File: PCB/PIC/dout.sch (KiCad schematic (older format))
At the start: 63 parts, among them J10 TB_1X3, J11 TB_1X2, J12 TB_1X3, J13 TB_1X3, J14 TB_1X2, J15 TB_1X3, K1 RELAY_TE_1461353-2, K2 RELAY_TE_1461353-2, K3 RELAY_TE_1461353-2, K4 RELAY_TE_1461353-2, Q11 NDS7002A, Q12 NDS7002A, Q2 FQT13N06L, Q3 FQT13N06L, Q4 FQT13N06L, Q5 FQT13N06L, Q6 NDS7002A, Q7 NDS7002A, U23 MCP1416, U27 MCP1416, U28 MCP1416, U29 MCP1416

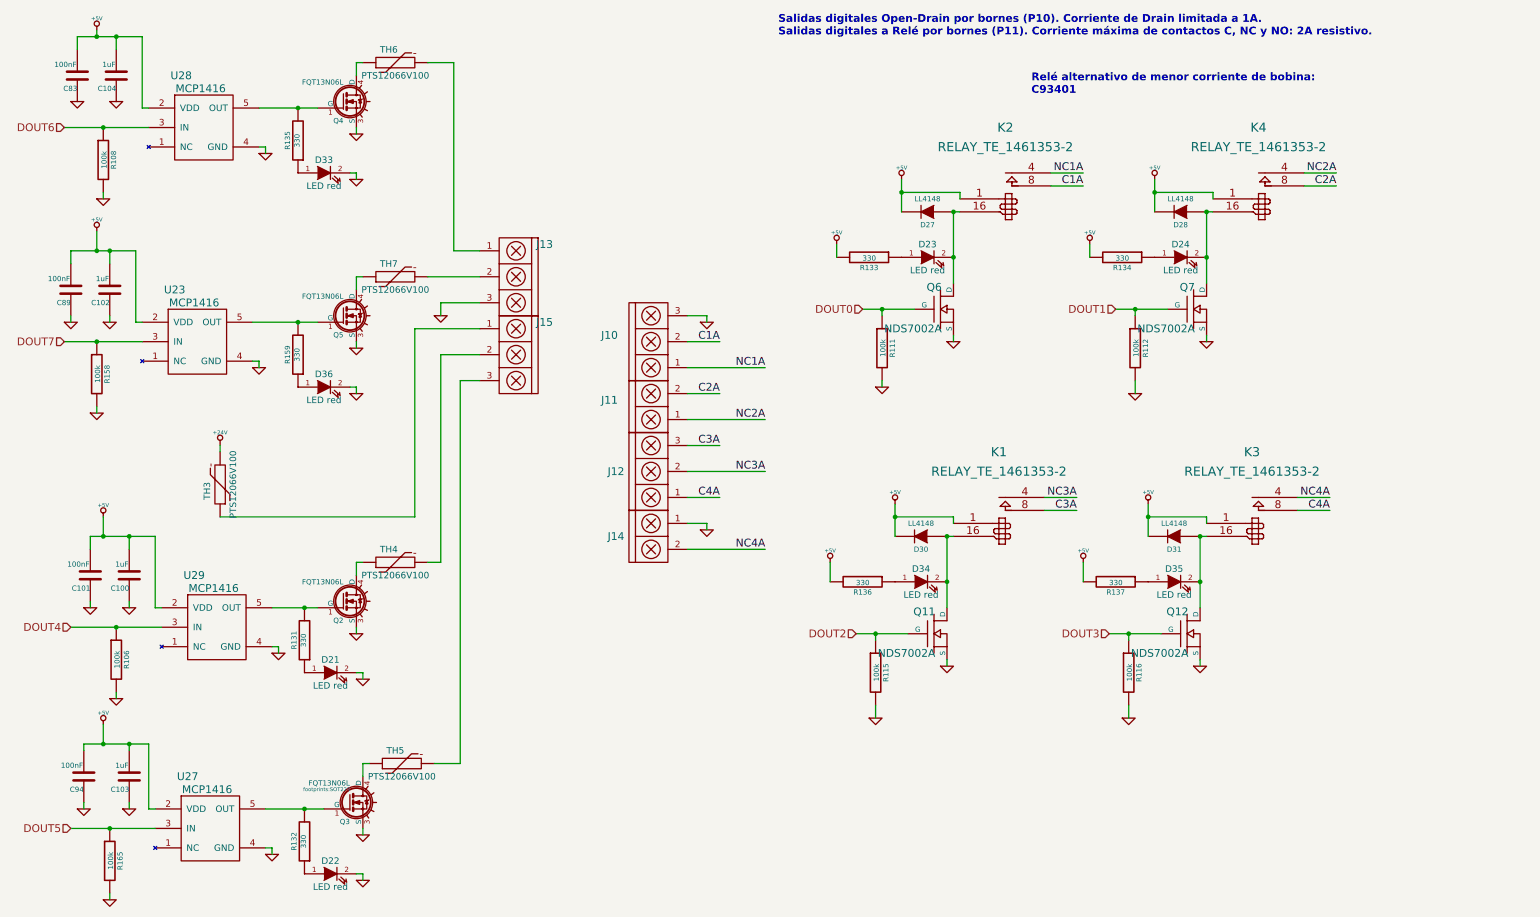
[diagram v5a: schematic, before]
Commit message: cambio en plano de masa eth - CIAA-PIC
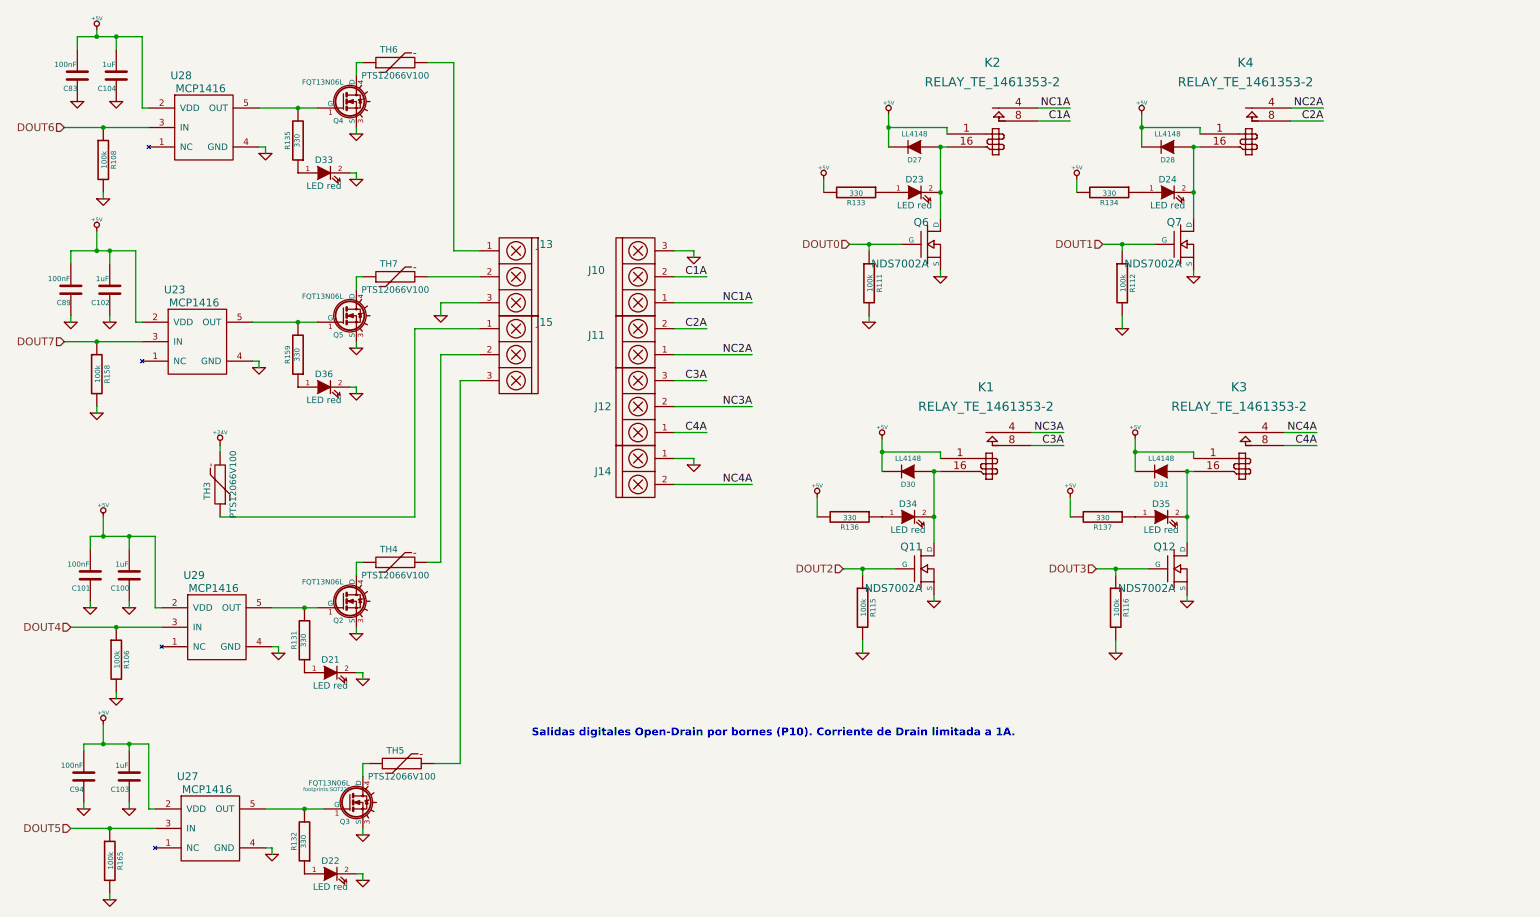
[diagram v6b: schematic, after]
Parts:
- C100, C101, C102, C103, C104, C83, C89, C94: footprint Capacitors_SMD:C_0603 -> footprints:c_0603
- D21, D22, D23, D24, D33, D34, D35, D36: footprint LEDs:LED_0603 -> footprints:LED-0603
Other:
- note added: "Salidas digitales Open-Drain por bornes (P10). Corriente de Drain limitada a 1A.\n"
- note removed: "Relé alternativo de menor corriente de bobina:\nC93401"
- note removed: "Salidas digitales Open-Drain por bornes (P10). Corriente de Drain limitada a 1A.\nSalidas digitales a Relé por bornes (P11). Corriente máxima de contactos C, NC y NO: 2A resistivo.\n"
- moved on the sheet: D23, D24, D27, D28, D30, D31, D34, D35, J10, J11, J12, J14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

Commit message: correccion pcb
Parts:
- Q11, Q12, Q6, Q7: footprint footprints:SOT23 -> footprints:SOT23GDS
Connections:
- net C1A: now also J10.1; no longer J10.2
- net C2A: now also J11.1; no longer J11.2
- net C3A: now also J12.2; no longer J12.3
- net C4A: now also J14.2; no longer J12.1
- net NC1A: now also J10.2; no longer J10.1
- net NC2A: now also J11.2; no longer J11.1
- net NC3A: now also J12.3; no longer J12.2
- net NC4A: now also J12.1; no longer J14.2
